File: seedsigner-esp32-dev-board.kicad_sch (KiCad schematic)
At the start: 4 parts, among them J1 Conn_01x05, U1 ESP32-S2-SAOLA-1M, U2 OV_CAMERA, U3 RASPBERRY_PI_3_MODEL_B+

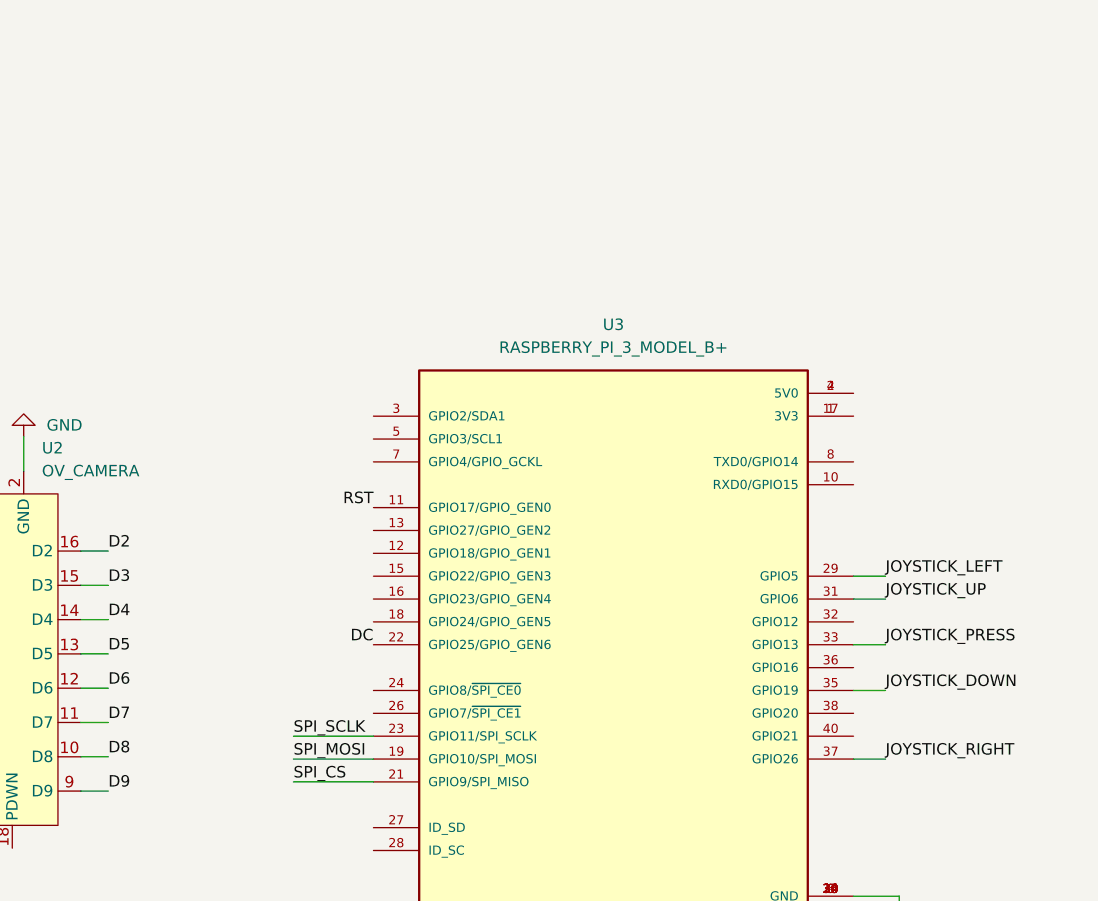
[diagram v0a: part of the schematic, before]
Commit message: update readme with links, add 3.3v to display and cap
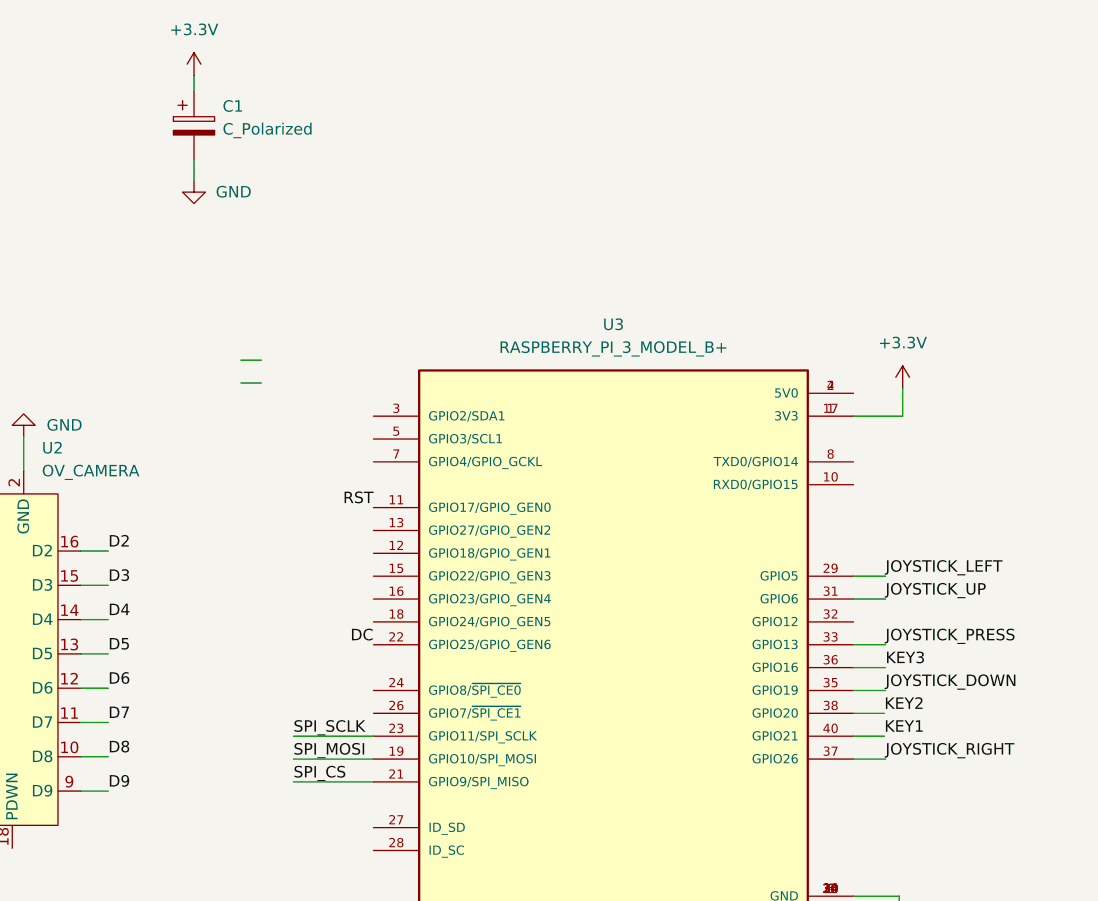
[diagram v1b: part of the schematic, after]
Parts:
- added C1: C_Polarized, Capacitor_THT:CP_Radial_D5.0mm_P2.50mm, symbol Device:C_Polarized
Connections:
- net +3.3V: now also U3.1 (3V3), U3.17 (3V3), C1.1
- net GND: now also C1.2
- net KEY1: now also U3.40 (GPIO21)
- net KEY2: now also U3.38 (GPIO20)
- net KEY3: now also U3.36 (GPIO16)
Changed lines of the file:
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@@
+    (stroke (width 0) (type default) (color 0 0 0 0))
+  )
+  (wire (pts (xy 250.063 115.824) (xy 246.634 115.824))
     (stroke (width 0) (type default) (color 0 0 0 0))
   )
@@
     (stroke (width 0) (type default) (color 0 0 0 0))
   )
+  (wire (pts (xy 246.634 82.804) (xy 252.095 82.804))
+    (stroke (width 0) (type default) (color 0 0 0 0))
+  )
+  (wire (pts (xy 180.848 79.121) (xy 178.562 79.121))
+    (stroke (width 0) (type default) (color 0 0 0 0))
+  )
   (wire (pts (xy 49.784 108.966) (xy 52.07 108.966))
     (stroke (width 0) (type default) (color 0 0 0 0))
@@
     (stroke (width 0) (type default) (color 0 0 0 0))
   )
+  (wire (pts (xy 173.355 44.958) (xy 173.355 46.736))
+    (stroke (width 0) (type default) (color 0 0 0 0))
+  )
   (wire (pts (xy 89.916 106.426) (xy 87.63 106.426))
     (stroke (width 0) (type default) (color 0 0 0 0))
@@
     (stroke (width 0) (type default) (color 0 0 0 0))
   )
+  (wire (pts (xy 180.848 76.581) (xy 178.562 76.581))
+    (stroke (width 0) (type default) (color 0 0 0 0))
+  )
   (wire (pts (xy 184.404 118.364) (xy 193.294 118.364))
     (stroke (width 0) (type default) (color 0 0 0 0))
@@
     (stroke (width 0) (type default) (color 0 0 0 0))
   )
+  (wire (pts (xy 250.19 110.744) (xy 246.634 110.744))
+    (stroke (width 0) (type default) (color 0 0 0 0))
+  )
   (wire (pts (xy 49.784 116.586) (xy 52.07 116.586))
     (stroke (width 0) (type default) (color 0 0 0 0))
@@
     (stroke (width 0) (type default) (color 0 0 0 0))
   )
+  (wire (pts (xy 252.095 82.804) (xy 252.095 79.756))
+    (stroke (width 0) (type default) (color 0 0 0 0))
+  )
   (wire (pts (xy 101.6 70.866) (xy 101.6 78.486))
     (stroke (width 0) (type default) (color 0 0 0 0))
@@
     (stroke (width 0) (type default) (color 0 0 0 0))
   )
+  (wire (pts (xy 173.355 56.642) (xy 173.355 54.356))
+    (stroke (width 0) (type default) (color 0 0 0 0))
+  )
   (wire (pts (xy 135.382 100.33) (xy 139.192 100.33))
     (stroke (width 0) (type default) (color 0 0 0 0))
@@
   )
   (wire (pts (xy 49.784 96.266) (xy 52.07 96.266))
+    (stroke (width 0) (type default) (color 0 0 0 0))
+  )
+  (wire (pts (xy 250.063 118.364) (xy 246.634 118.364))
     (stroke (width 0) (type default) (color 0 0 0 0))
   )
@@
     (effects (font (size 1.27 1.27)) (justify right bottom))
   )
+  (label "KEY2" (at 250.063 115.824 0)
+    (effects (font (size 1.27 1.27)) (justify left bottom))
+  )
   (label "RST" (at 49.784 93.726 180)
     (effects (font (size 1.27 1.27)) (justify right bottom))
@@
     (effects (font (size 1.27 1.27)) (justify right bottom))
   )
+  (label "KEY3" (at 250.19 110.744 0)
+    (effects (font (size 1.27 1.27)) (justify left bottom))
+  )
   (label "DC" (at 193.294 108.204 180)
     (effects (font (size 1.27 1.27)) (justify right bottom))
@@
     (effects (font (size 1.27 1.27)) (justify left bottom))
   )
+  (label "KEY1" (at 250.063 118.364 0)
+    (effects (font (size 1.27 1.27)) (justify left bottom))
+  )
   (label "XCLK" (at 52.07 98.806 180)
     (effects (font (size 1.27 1.27)) (justify right bottom))
@@
   (label "JOYSTICK_PRESS" (at 49.784 131.826 180)
     (effects (font (size 1.27 1.27)) (justify right bottom))
+  )
+  (symbol (lib_id "Device:C_Polarized") (at 173.355 50.546 0) (unit 1)
+    (in_bom yes) (on_board yes) (fields_autoplaced)
+    (property "Reference" "C1" (id 0) (at 176.53 48.3869 0)
+      (effects (font (size 1.27 1.27)) (justify left))
+    )
+    (property "Value" "C_Polarized" (id 1) (at 176.53 50.9269 0)
+      (effects (font (size 1.27 1.27)) (justify left))
+    )
+    (property "Footprint" "Capacitor_THT:CP_Radial_D5.0mm_P2.50mm" (id 2) (at 174.3202 54.356 0)
+      (effects (font (size 1.27 1.27)) hide)
+    )
+    (property "Datasheet" "~" (id 3) (at 173.355 50.546 0)
+      (effects (font (size 1.27 1.27)) hide)
+    )
+    (pin "1")
+    (pin "2")
   )
   (symbol (lib_id "SeedSigner:OV_CAMERA") (at 150.622 97.79 0) (unit 1)
@@
     (pin "8")
     (pin "9")
+  )
+  (symbol (lib_id "power:+3.3V") (at 252.095 79.756 0) (unit 1)
+    (in_bom yes) (on_board yes) (fields_autoplaced)
+    (property "Reference" "#PWR09" (id 0) (at 252.095 83.566 0)
+      (effects (font (size 1.27 1.27)) hide)
+    )
+    (property "Value" "+3.3V" (id 1) (at 252.095 74.676 0))
+    (property "Footprint" "" (id 2) (at 252.095 79.756 0)
+      (effects (font (size 1.27 1.27)) hide)
+    )
+    (property "Datasheet" "" (id 3) (at 252.095 79.756 0)
+      (effects (font (size 1.27 1.27)) hide)
+    )
+    (pin "1")
   )
   (symbol (lib_id "SeedSigner:RASPBERRY_PI_3_MODEL_B+") (at 221.234 103.124 0) (unit 1)
@@
     (pin "TX")
   )
+  (symbol (lib_id "power:GND") (at 173.355 56.642 0) (unit 1)
+    (in_bom yes) (on_board yes) (fields_autoplaced)
+    (property "Reference" "#PWR08" (id 0) (at 173.355 62.992 0)
+      (effects (font (size 1.27 1.27)) hide)
+    )
+    (property "Value" "GND" (id 1) (at 175.768 57.9119 0)
+      (effects (font (size 1.27 1.27)) (justify left))
+    )
+    (property "Footprint" "" (id 2) (at 173.355 56.642 0)
+      (effects (font (size 1.27 1.27)) hide)
+    )
+    (property "Datasheet" "" (id 3) (at 173.355 56.642 0)
+      (effects (font (size 1.27 1.27)) hide)
+    )
+    (pin "1")
+  )
   (symbol (lib_id "power:+3.3V") (at 96.52 70.866 0) (unit 1)
     (in_bom yes) (on_board yes) (fields_autoplaced)
@@
     )
     (property "Datasheet" "" (id 3) (at 96.52 70.866 0)
+      (effects (font (size 1.27 1.27)) hide)
+    )
+    (pin "1")
+  )
+  (symbol (lib_id "power:+3.3V") (at 173.355 44.958 0) (unit 1)
+    (in_bom yes) (on_board yes) (fields_autoplaced)
+    (property "Reference" "#PWR07" (id 0) (at 173.355 48.768 0)
+      (effects (font (size 1.27 1.27)) hide)
+    )
+    (property "Value" "+3.3V" (id 1) (at 173.355 39.878 0))
+    (property "Footprint" "" (id 2) (at 173.355 44.958 0)
+      (effects (font (size 1.27 1.27)) hide)
+    )
+    (property "Datasheet" "" (id 3) (at 173.355 44.958 0)
       (effects (font (size 1.27 1.27)) hide)
     )
@@
       (reference "#PWR06") (unit 1) (value "GND") (footprint "")
     )
+    (path "/d38510f1-2168-4a26-a970-b83a1946335b"
+      (reference "#PWR07") (unit 1) (value "+3.3V") (footprint "")
+    )
+    (path "/966f6026-6b2e-4234-b132-3cd0fb4c098a"
+      (reference "#PWR08") (unit 1) (value "GND") (footprint "")
+    )
+    (path "/3270eb70-5b3d-4716-be93-68fc7adb56d5"
+      (reference "#PWR09") (unit 1) (value "+3.3V") (footprint "")
+    )
+    (path "/0109e084-0876-4092-9baa-19db7962d473"
+      (reference "C1") (unit 1) (value "C_Polarized") (footprint "Capacitor_THT:CP_Radial_D5.0mm_P2.50mm")
+    )
     (path "/5193b365-d3e5-416b-aea2-2e44cdead9a6"

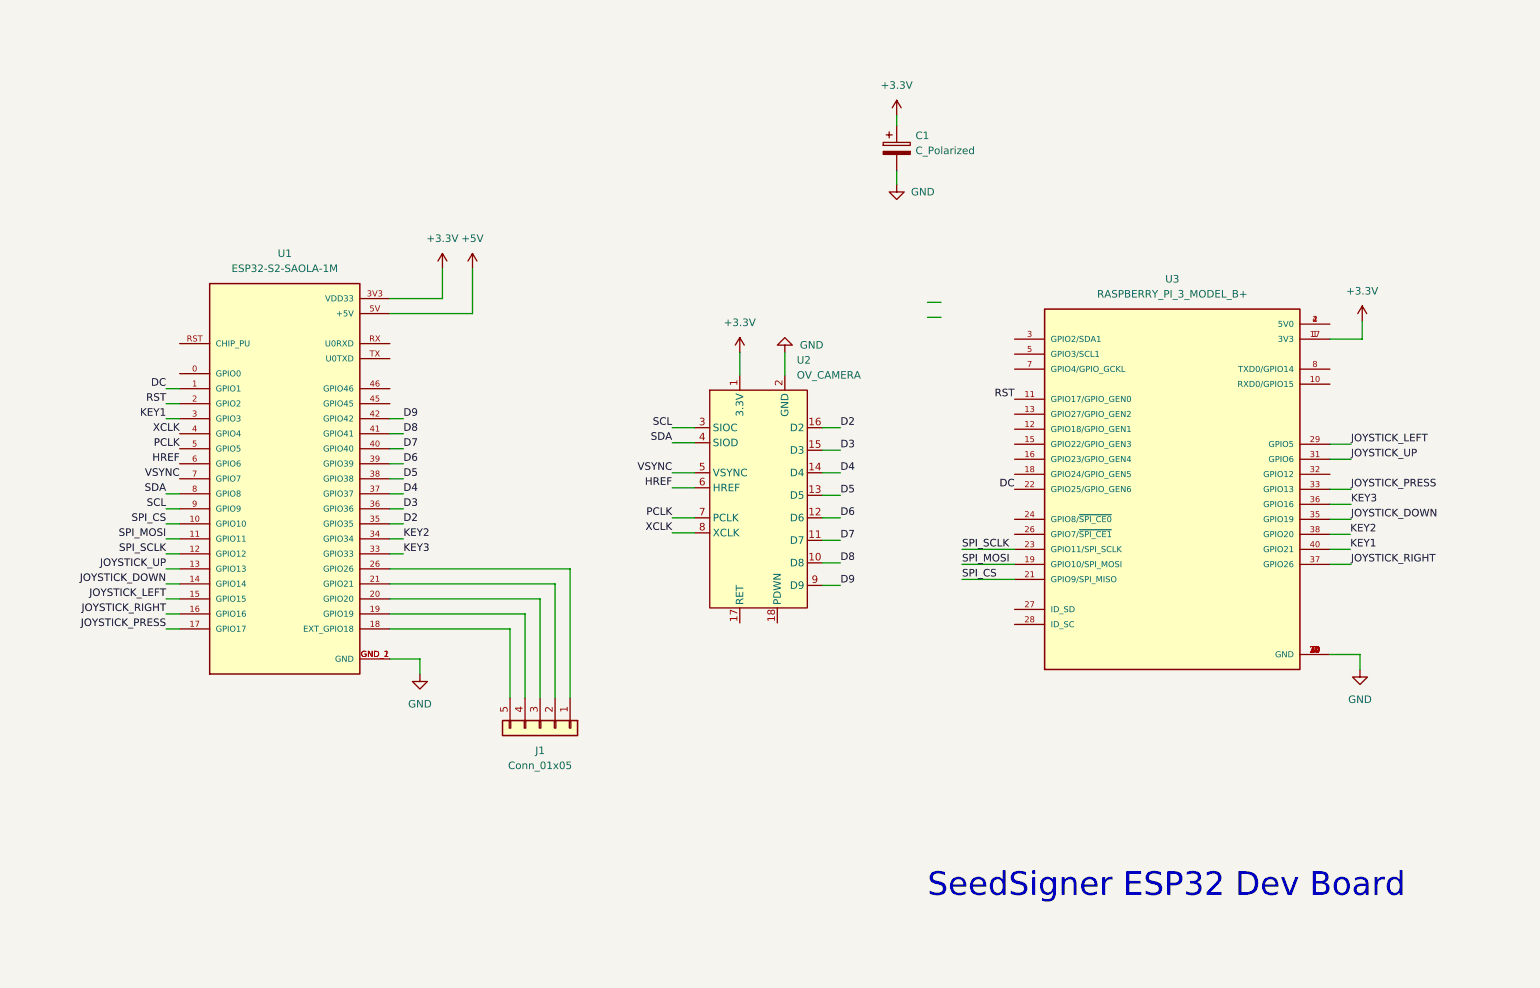
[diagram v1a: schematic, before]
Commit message: rewire all the pins to make routing cleaner
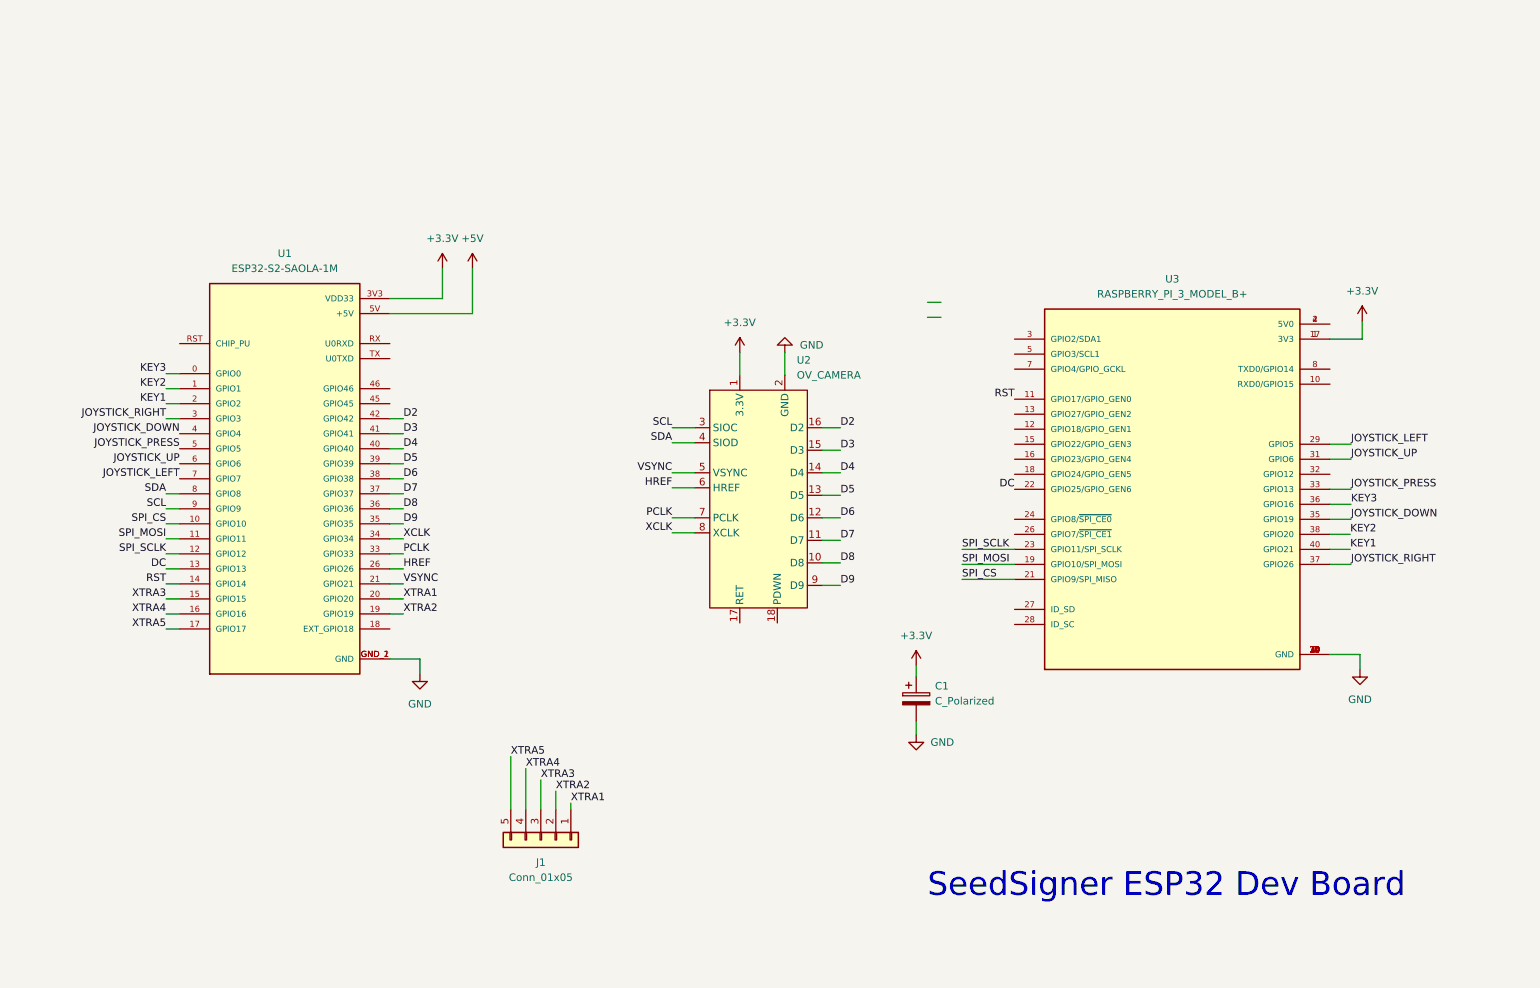
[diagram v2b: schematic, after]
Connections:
- net D2: now also U1.42 (GPIO42); no longer U1.35 (GPIO35)
- net D3: now also U1.41 (GPIO41); no longer U1.36 (GPIO36)
- net D4: now also U1.40 (GPIO40); no longer U1.37 (GPIO37)
- net D5: now also U1.39 (GPIO39); no longer U1.38 (GPIO38)
- net D6: now also U1.38 (GPIO38); no longer U1.39 (GPIO39)
- net D7: now also U1.37 (GPIO37); no longer U1.40 (GPIO40)
- net D8: now also U1.36 (GPIO36); no longer U1.41 (GPIO41)
- net D9: now also U1.35 (GPIO35); no longer U1.42 (GPIO42)
- net DC: now also U1.13 (GPIO13); no longer U1.1 (GPIO1)
- net HREF: now also U1.26 (GPIO26); no longer U1.6 (GPIO6)
- net JOYSTICK_DOWN: now also U1.4 (GPIO4); no longer U1.14 (GPIO14)
- net JOYSTICK_LEFT: now also U1.7 (GPIO7); no longer U1.15 (GPIO15)
- net JOYSTICK_PRESS: now also U1.5 (GPIO5); no longer U1.17 (GPIO17)
- net JOYSTICK_RIGHT: now also U1.3 (GPIO3); no longer U1.16 (GPIO16)
- net JOYSTICK_UP: now also U1.6 (GPIO6); no longer U1.13 (GPIO13)
- net KEY1: now also U1.2 (GPIO2); no longer U1.3 (GPIO3)
- net KEY2: now also U1.1 (GPIO1); no longer U1.34 (GPIO34)
- net KEY3: now also U1.0 (GPIO0); no longer U1.33 (GPIO33)
- net PCLK: now also U1.33 (GPIO33); no longer U1.5 (GPIO5)
- net RST: now also U1.14 (GPIO14); no longer U1.2 (GPIO2)
- net VSYNC: now also U1.21 (GPIO21); no longer U1.7 (GPIO7)
- net XCLK: now also U1.34 (GPIO34); no longer U1.4 (GPIO4)
- net XTRA1: now reaches J1.1 (Pin_1)
- net XTRA1: now also U1.20 (GPIO20); no longer U1.26 (GPIO26)
- net XTRA2: now reaches J1.2 (Pin_2)
- net XTRA2: now also U1.19 (GPIO19); no longer U1.21 (GPIO21)
- net XTRA3: now reaches J1.3 (Pin_3)
- net XTRA3: now also U1.15 (GPIO15); no longer U1.20 (GPIO20)
- net XTRA4: now reaches J1.4 (Pin_4)
- net XTRA4: now also U1.16 (GPIO16); no longer U1.19 (GPIO19)
- net at U1.18 (EXT_GPIO18): no longer J1.5 (Pin_5)
- new net XTRA5: J1.5 (Pin_5), U1.17 (GPIO17)
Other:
- moved on the sheet: C1, J1

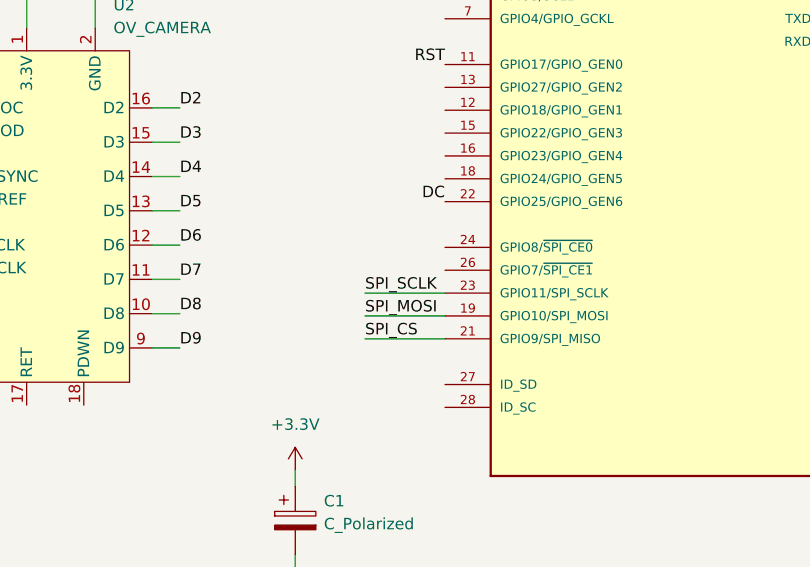
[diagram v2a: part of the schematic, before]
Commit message: fix small wiring issue, add mounting hole for lcd, add silkscreen
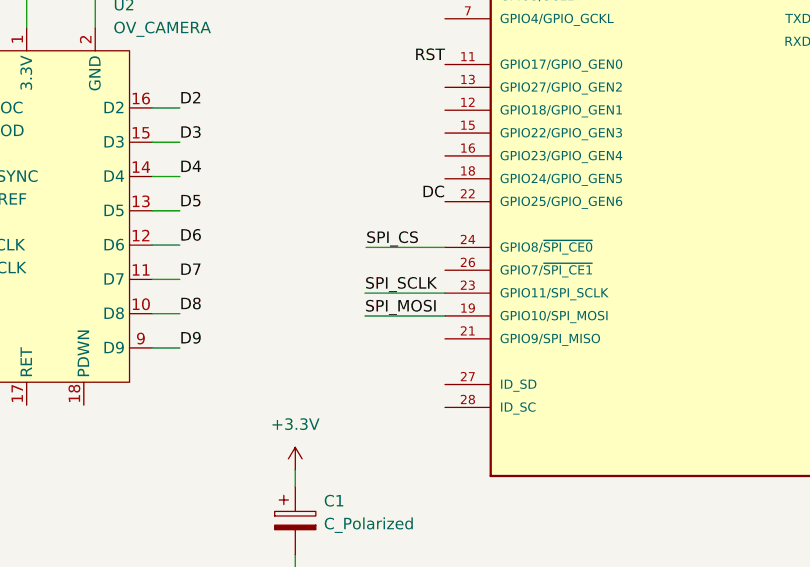
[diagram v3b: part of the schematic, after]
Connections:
- net SPI_CS: now also U3.24 (GPIO8/~{SPI_CE0}); no longer U3.21 (GPIO9/SPI_MISO)
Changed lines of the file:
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@@
     (stroke (width 0) (type default) (color 0 0 0 0))
   )
-  (wire (pts (xy 184.404 123.444) (xy 193.294 123.444))
+  (wire (pts (xy 184.531 113.284) (xy 193.294 113.284))
     (stroke (width 0) (type default) (color 0 0 0 0))
   )
@@
     (effects (font (size 1.27 1.27)) (justify left bottom))
   )
-  (label "SPI_CS" (at 184.404 123.444 0)
+  (label "SPI_CS" (at 184.531 113.284 0)
     (effects (font (size 1.27 1.27)) (justify left bottom))
   )
